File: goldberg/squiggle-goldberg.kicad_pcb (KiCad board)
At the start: 2 copper layers, 116 x 115.3 mm, 54 parts, among them P1 OLED, SW1 switch, SW10 switch, SW11 switch, SW12 switch, SW13 switch, SW14 switch, SW15-1 switch, SW15-2 switch, SW16 switch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

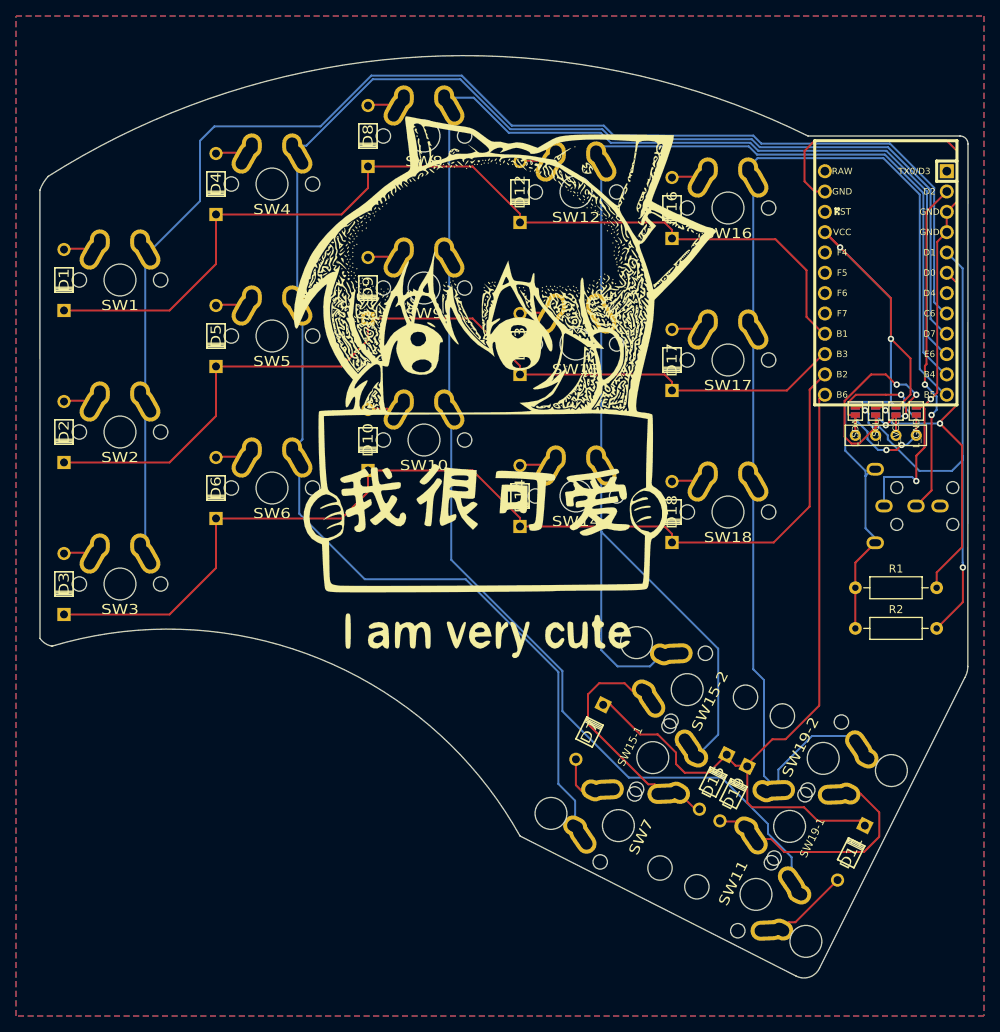
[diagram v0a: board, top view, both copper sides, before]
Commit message: Added LEDs and RESET button
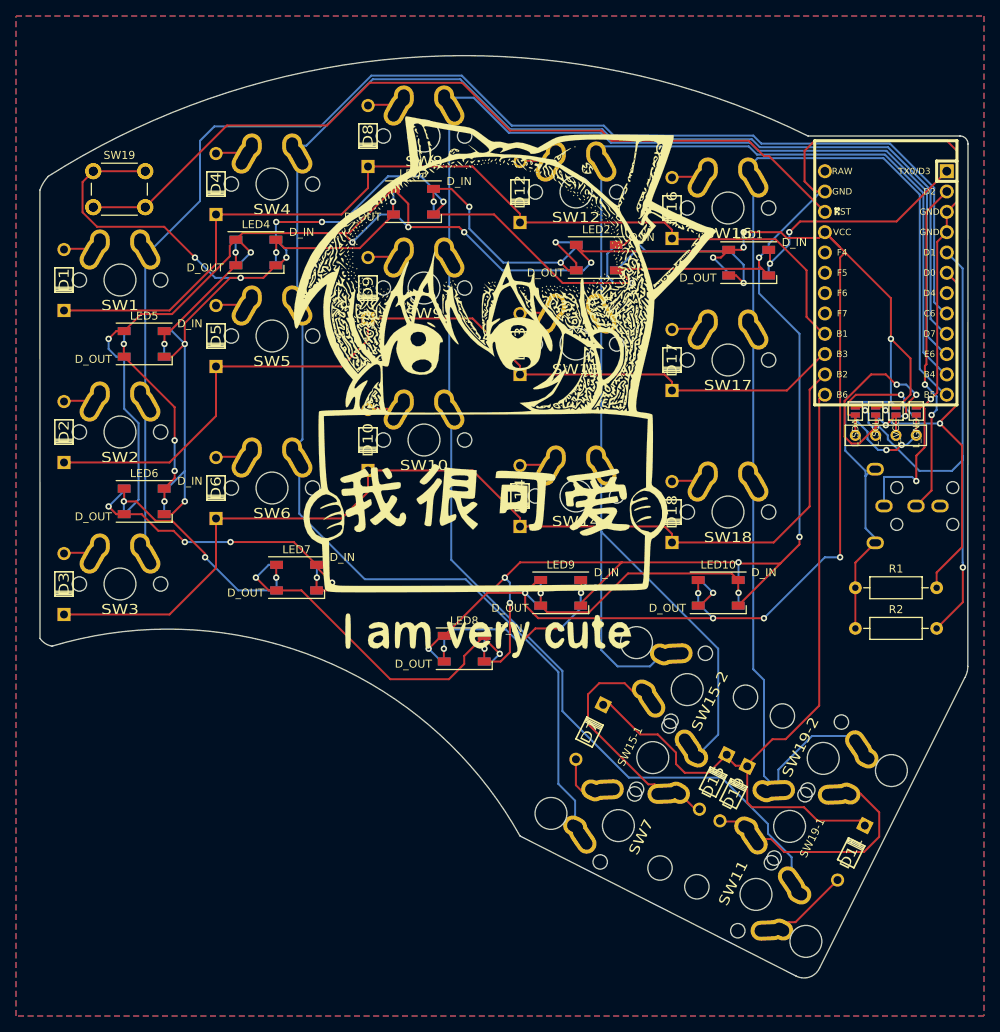
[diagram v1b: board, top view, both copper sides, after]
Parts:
- added LED1: WS2812B, footprints:LED_WS2812B_4Pad, F.Cu at (108.6, 36.8)
- added LED10: WS2812B, footprints:LED_WS2812B_4Pad, F.Cu at (104.8, 78.1)
- added LED2: WS2812B, footprints:LED_WS2812B_4Pad, F.Cu at (89.5, 36.2)
- added LED3: WS2812B, footprints:LED_WS2812B_4Pad, F.Cu at (66.7, 29.2)
- added LED4: WS2812B, footprints:LED_WS2812B_4Pad, F.Cu at (47.0, 35.6)
- added LED5: WS2812B, footprints:LED_WS2812B_4Pad, F.Cu at (33.0, 47.0)
- added LED6: WS2812B, footprints:LED_WS2812B_4Pad, F.Cu at (33.0, 66.7)
- added LED7: WS2812B, footprints:LED_WS2812B_4Pad, F.Cu at (52.1, 76.2)
- added LED8: WS2812B, footprints:LED_WS2812B_4Pad, F.Cu at (73.0, 85.1)
- added LED9: WS2812B, footprints:LED_WS2812B_4Pad, F.Cu at (85.1, 78.1)
- added SW15: SW_Push, Button_Switch_THT:SW_PUSH_6mm_H5mm, B.Cu at (33.1, 25.4)
- added SW19: SW_Push, Button_Switch_THT:SW_PUSH_6mm_H5mm, F.Cu at (26.7, 25.4)
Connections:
- U2 pad 1: Net-(U2-Pad1) -> LED
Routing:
- net GND: track 81.5 -> 412.4 mm, vias 2 -> 19
- net VCC: track 99.5 -> 378.1 mm, vias 2 -> 19
- net Net-(SW15-Pad2): track 0.00 -> 104.6 mm
- net Net-(LED7-Pad2): track 0.00 -> 45.3 mm, vias 0 -> 2
- net Net-(LED6-Pad2): track 0.00 -> 37.4 mm, vias 0 -> 4
- net Net-(LED2-Pad2): track 0.00 -> 37.2 mm, vias 0 -> 4
- net Net-(LED10-Pad4): track 0.00 -> 33.8 mm, vias 0 -> 2
- net LED: track 0.00 -> 31.1 mm, vias 0 -> 2
- net Net-(LED1-Pad2): track 0.00 -> 27.1 mm, vias 0 -> 2
- net LED_CONT: track 0.00 -> 26.8 mm, vias 0 -> 4
- net Net-(LED8-Pad2): track 0.00 -> 26.8 mm, vias 0 -> 4
- net Net-(LED3-Pad2): track 0.00 -> 23.3 mm, vias 0 -> 2
- net Net-(LED4-Pad2): track 0.00 -> 18.8 mm, vias 0 -> 2
- net Net-(LED10-Pad2): track 0.00 -> 5.06 mm, vias 0 -> 1

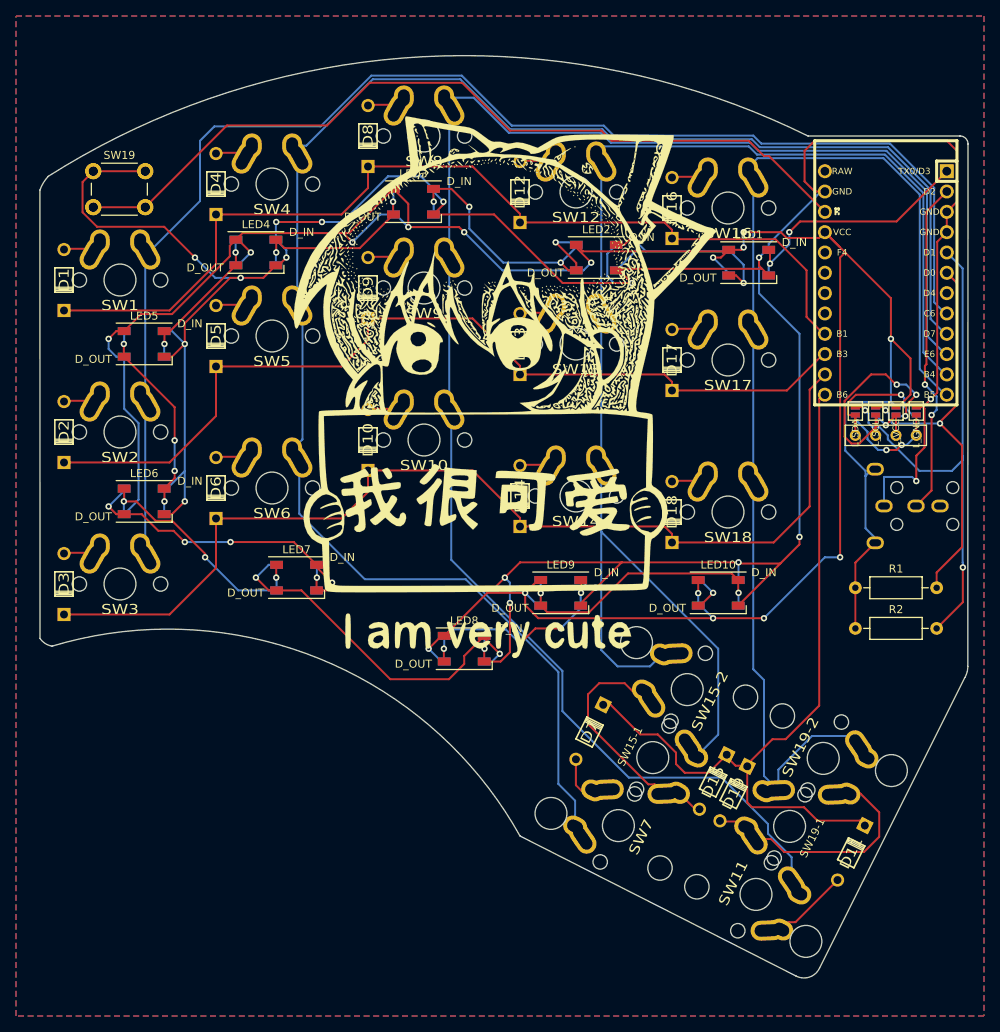
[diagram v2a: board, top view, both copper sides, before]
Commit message: Added GND fill to both Cu layers
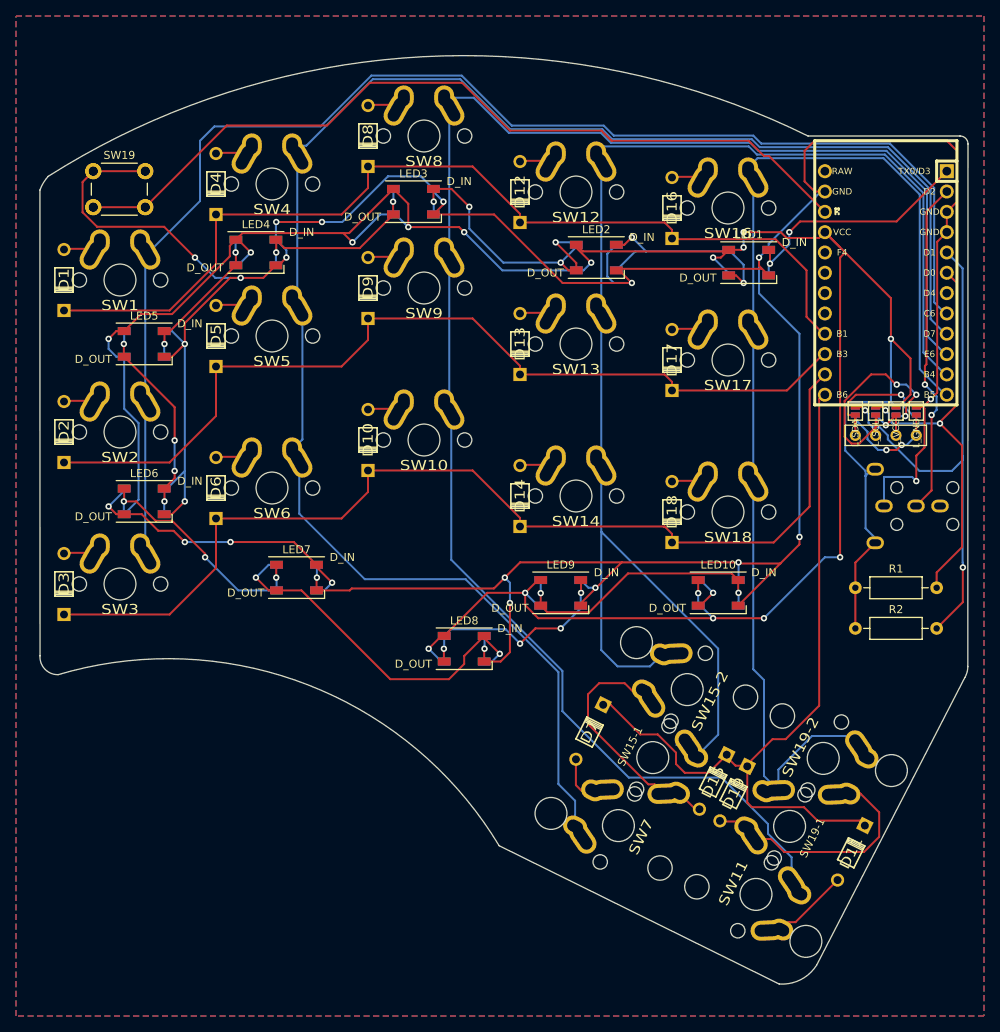
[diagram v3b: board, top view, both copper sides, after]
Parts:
- removed G***: LOGO, footprints:mokou-cute
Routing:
- added copper zone on B.Cu, net GND
- added copper zone on F.Cu, net GND
- removed copper zone on B.Cu, net (none)
- removed copper zone on F.Cu, net (none)
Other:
- board size 116 x 115.3 mm -> 116 x 116.1 mm
